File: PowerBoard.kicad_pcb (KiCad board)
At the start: 2 copper layers, 21.7 x 14.5 mm, 8 parts

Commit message: add text.
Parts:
- PB1: moved to B.Cu
- turned PB1 to 180 degrees

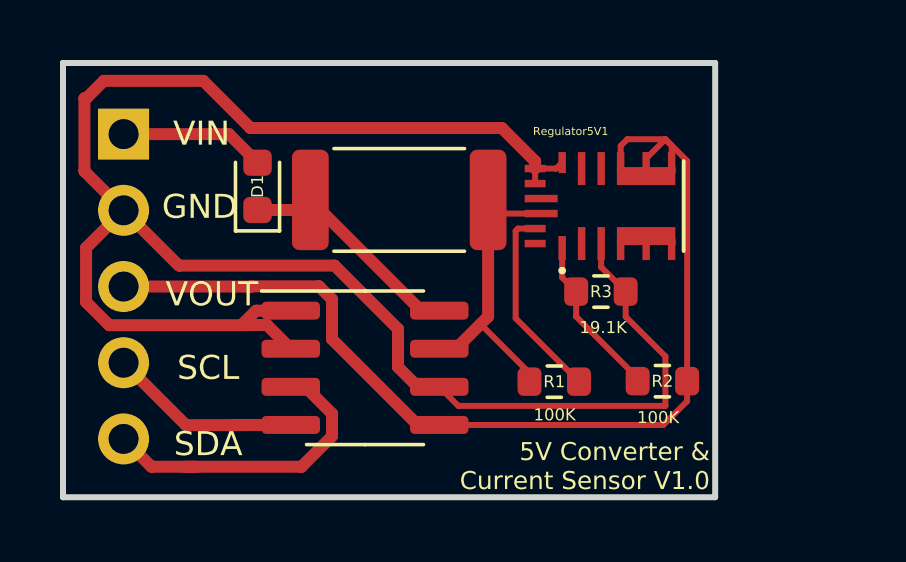
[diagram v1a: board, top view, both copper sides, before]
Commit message: add additional AAM resistor and increment board version. Instructions for 3.3V output rather than 5V if desired.
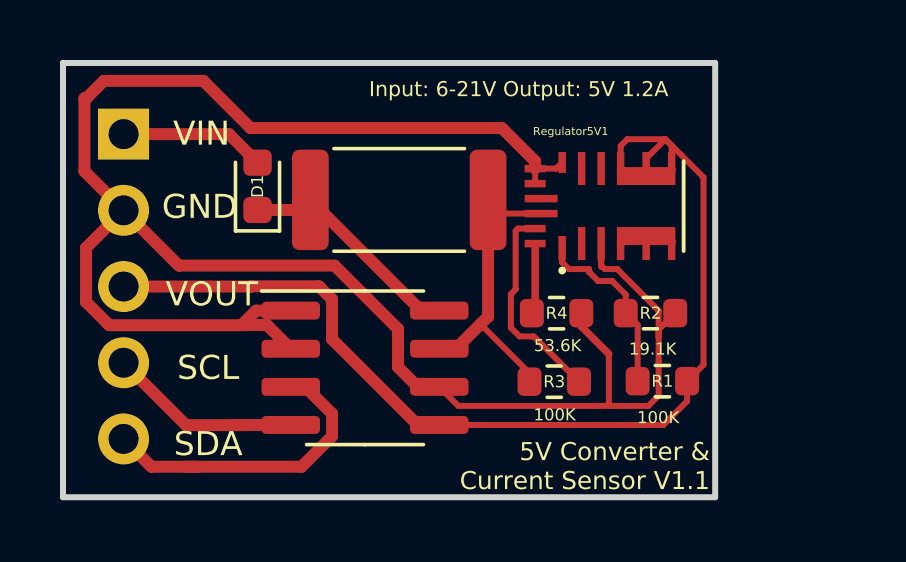
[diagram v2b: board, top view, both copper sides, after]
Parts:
- added R4: 53.6K, Resistor_SMD:R_0603_1608Metric, F.Cu at (131.0, 59.1)
- moved R2 1.80 mm to (134.1, 59.1)
- renumbered R2 to R1, R3 to R2, R1 to R3
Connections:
- Regulator5V1 pad 18: unconnected-(Regulator5V1-Pad18) -> Net-(R4-Pad1)
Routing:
- net GND: track 63.2 -> 68.2 mm
- net Net-(R4-Pad1): track 0.00 -> 2.37 mm
- net Net-(R1-Pad2): track 5.48 -> 6.15 mm
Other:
- board text added: "5V Converter & Current Sensor V1.1"
- board text added: "Input: 6-21V Output: 5V 1.2A"
- board text added: "To configure output, select your resistors as follows. Assuming ~12V Input. Max 1.2A. For more details review the datasheet for MPM3610A. Output R1 R2 R3 R4 5V 100k 19.1K 100K 53.6K 3.3V 75k 24K 100K 39K"
- board text removed: "5V Converter & Current Sensor V1.0"

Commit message: version 1.2.
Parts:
- removed D1: D_Schottky, Diode_SMD:D_0603_1608Metric
- added A0: A0, Jumper:SolderJumper-2_P1.3mm_Open_Pad1.0x1.5mm, F.Cu at (133.8, 63.8)
- added A1: A1, Jumper:SolderJumper-2_P1.3mm_Open_Pad1.0x1.5mm, F.Cu at (130.3, 63.8)
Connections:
- CURRENT_MAIN1 pad 1: GND -> Net-(CURRENT_MAIN1-Pad1)
- CURRENT_MAIN1 pad 2: GND -> Net-(CURRENT_MAIN1-Pad2)
- PB1 pad 1: Net-(D1-Pad2) -> Net-(CURRENT_MAIN1-Pad8)
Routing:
- net Net-(CURRENT_MAIN1-Pad2): track 0.00 -> 16.0 mm
- net GND: track 68.2 -> 55.1 mm
- net Net-(CURRENT_MAIN1-Pad1): track 0.00 -> 9.47 mm
- net Net-(CURRENT_MAIN1-Pad8): track 8.40 -> 14.1 mm
- net Net-(D1-Pad2): track 4.86 -> 0.00 mm
- net +5V: track 35.3 -> 37.8 mm
- net /SDA: track 10.6 -> 10.0 mm
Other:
- board text added: "5V Buck Converter & Current Sensor V1.2 The default I2C address for this device is 0x40. You can adjust the address of the device by shorting jumpers A0 and A1. See the table in the INA219 datasheet for more details. I2C Address A0 A1 0x40 Open Open 0x41 Open Closed 0x44 Closed Open It is possible to adjust the voltage output. This can be achieved by swapping out the resistors as defined in the f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"
- board text added: "5V DC-DC Converter & Current Sensor V1.2"
- board text removed: "5V Converter & Current Sensor V1.1"
- board text removed: "To configure output, select your resistors as follows. Assuming ~12V Input. Max 1.2A. For more details review the datasheet for MPM3610A. Output R1 R2 R3 R4 5V 100k 19.1K 100K 53.6K 3.3V 75k 24K 100K 39K"

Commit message: update to 1.3.
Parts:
- added C1: 10uF, Capacitor_SMD:C_0603_1608Metric_Pad1.08x0.95mm_HandSolder, F.Cu at (130.9, 54.4)
- added C2: 22uF, Capacitor_SMD:C_0603_1608Metric_Pad1.08x0.95mm_HandSolder, F.Cu at (137.4, 59.1)
- added R5: 10K, Resistor_SMD:R_0603_1608Metric, F.Cu at (137.6, 61.4)
- added R6: 10K, Resistor_SMD:R_0603_1608Metric, F.Cu at (137.1, 63.6)
- moved Regulator5V1 2.37 mm to (135.1, 55.6)
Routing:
- net Net-(A1-Pad1): track 9.47 -> 23.4 mm, vias 0 -> 2
- net GND: track 55.1 -> 61.4 mm
- net +5V: track 37.8 -> 41.1 mm
- net Net-(C1-Pad1): track 10.9 -> 13.3 mm
- net Net-(A0-Pad1): track 16.0 -> 17.9 mm
- net Net-(R1-Pad2): track 6.15 -> 4.67 mm
- net Net-(R3-Pad2): track 6.99 -> 8.21 mm
- net Net-(R4-Pad1): track 2.37 -> 3.43 mm
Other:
- board size 21.7 x 14.5 mm -> 24.9 x 14.5 mm
- board text added: "5V DC-DC Converter & Current Sensor V1.3"
- board text removed: "5V Buck Converter & Current Sensor V1.2 The default I2C address for this device is 0x40. You can adjust the address of the device by shorting jumpers A0 and A1. See the table in the INA219 datasheet for more details. I2C Address A0 A1 0x40 Open Open 0x41 Open Closed 0x44 Closed Open It is possible to adjust the voltage output. This can be achieved by swapping out the resistors as defined in the f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"
- board text removed: "5V DC-DC Converter & Current Sensor V1.2"
